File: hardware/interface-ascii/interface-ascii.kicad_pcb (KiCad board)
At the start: 2 copper layers, 88.9 x 132.1 mm, 51 parts, among them J1 Apple 2, J2 Apple 1, J3 UART, J4 Conn_01x05, J5 ISP header, J6 Keyboard, J7 SOL-20, SW1 Options, U1 ATmega328P, U2 74LS166, U3 74LS138, U4 74LS138, U5 74LS04

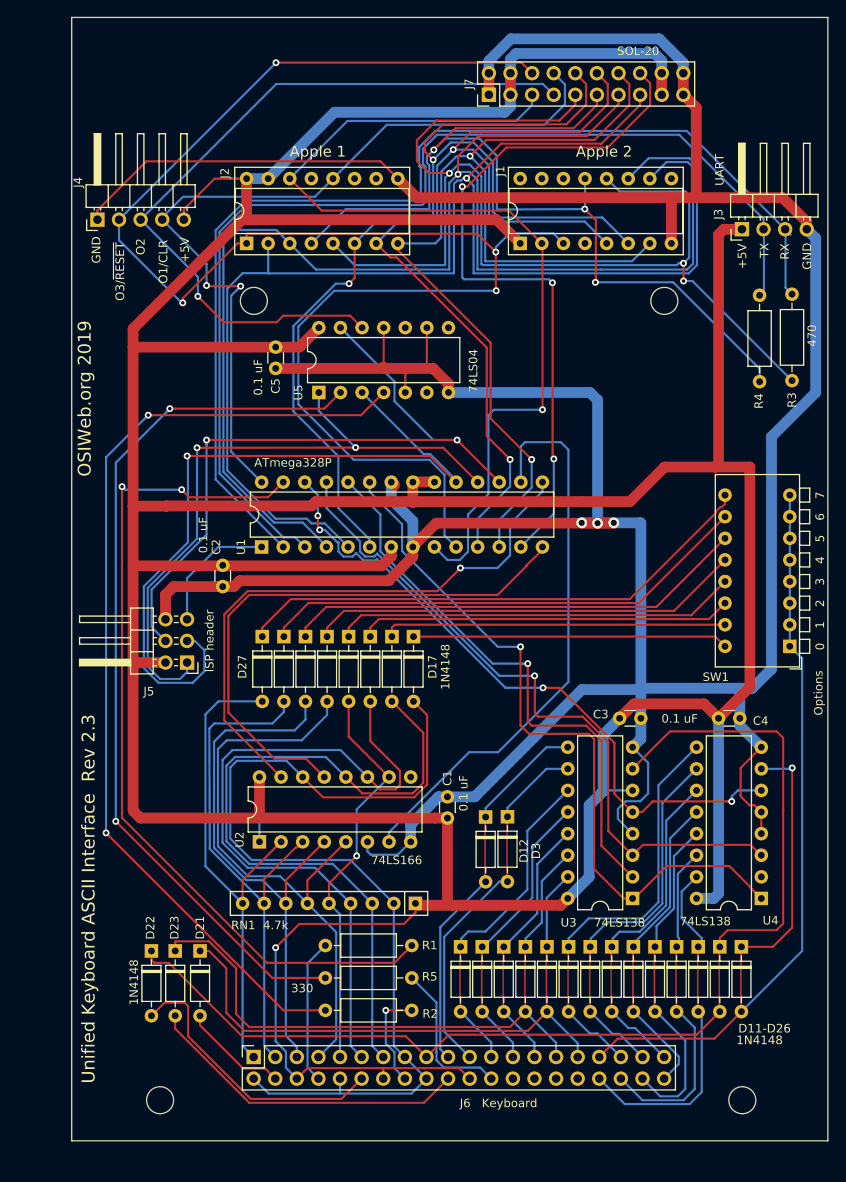
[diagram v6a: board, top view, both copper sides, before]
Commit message: PCB cleanups
- swap numbering of row select protection diodes for cleaner PCB labeling
- clarify labeling on GPIO pins on the MCU
- bump rev to 2.4 to indicate work in progress. Release will be 2.5.
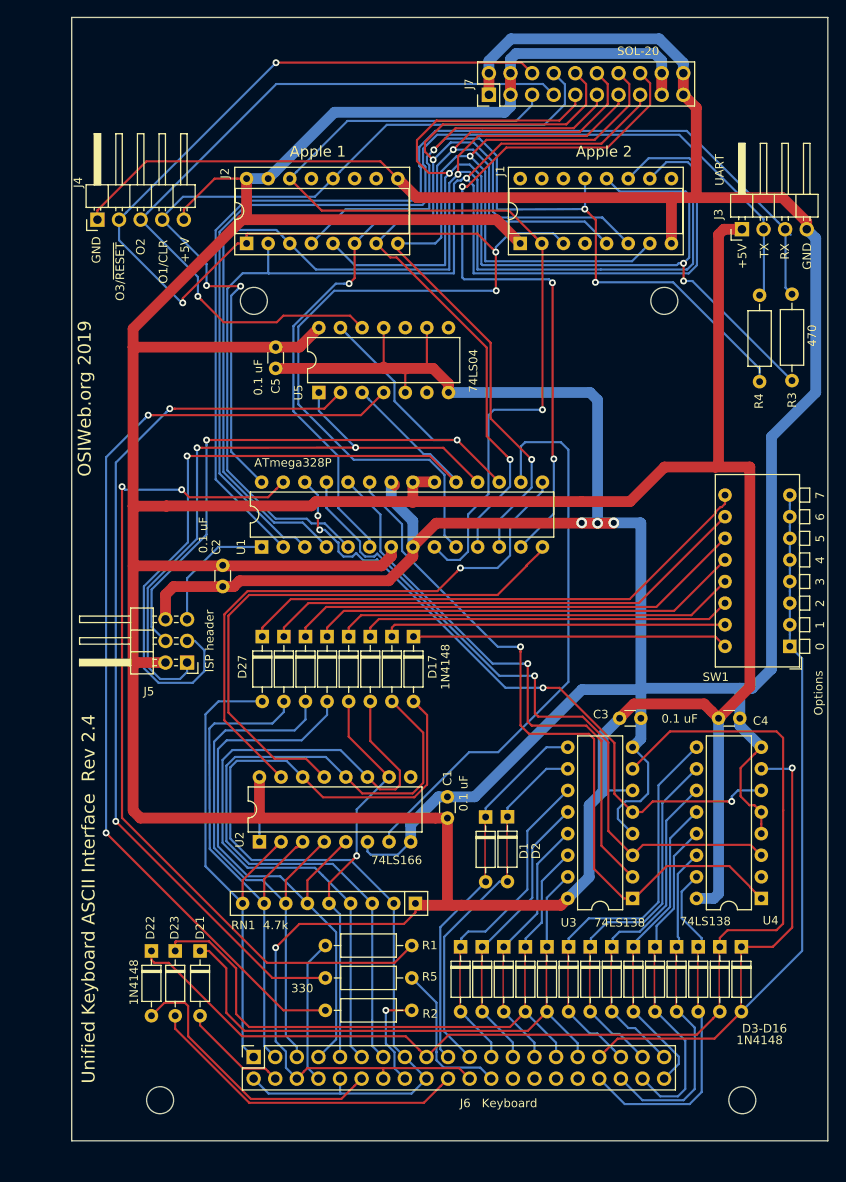
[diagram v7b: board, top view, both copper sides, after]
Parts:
- renumbered D12 to D1, D1 to D12, D3 to D2, D2 to D3
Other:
- board text added: "D3-D16"
- board text added: "Unified Keyboard ASCII Interface Rev 2.4"
- board text removed: "D11-D26"
- board text removed: "Unified Keyboard ASCII Interface Rev 2.3"
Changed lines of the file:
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@@
     (title "Unified Retro Keyboard")
     (date 2019-12-13)
-    (rev 2.3)
+    (rev 2.4)
   )
   (layers
@@
     (descr "Diode, DO-35_SOD27 series, Axial, Horizontal, pin pitch=7.62mm, , length*diameter=4*2mm^2, , http://www.diodes.com/_files/packages/DO-35.pdf")
     (tags "Diode DO-35_SOD27 series Axial Horizontal pin pitch 7.62mm  length 4mm diameter 2mm")
-    (fp_text reference D12 (at 3.9878 -4.4958 90) (layer F.SilkS)
+    (fp_text reference D1 (at 3.9878 -4.4958 90) (layer F.SilkS)
       (effects (font (size 1 1) (thickness 0.15)))
     )
@@
     )
     (pad 1 thru_hole rect (at 0 0 270) (size 1.6 1.6) (drill 0.8) (layers *.Cu *.Mask)
-      (net 48 "Net-(D12-Pad1)"))
+      (net 68 "Net-(D1-Pad1)"))
     (pad 2 thru_hole oval (at 7.62 0 270) (size 1.6 1.6) (drill 0.8) (layers *.Cu *.Mask)
       (net 24 /Row6))
@@
     (descr "Diode, DO-35_SOD27 series, Axial, Horizontal, pin pitch=7.62mm, , length*diameter=4*2mm^2, , http://www.diodes.com/_files/packages/DO-35.pdf")
     (tags "Diode DO-35_SOD27 series Axial Horizontal pin pitch 7.62mm  length 4mm diameter 2mm")
-    (fp_text reference D3 (at 4.0132 -3.3528 90) (layer F.SilkS)
+    (fp_text reference D2 (at 4.0132 -3.3528 90) (layer F.SilkS)
       (effects (font (size 1 1) (thickness 0.15)))
     )
@@
     )
     (pad 1 thru_hole rect (at 0 0 270) (size 1.6 1.6) (drill 0.8) (layers *.Cu *.Mask)
-      (net 60 "Net-(D3-Pad1)"))
+      (net 69 "Net-(D2-Pad1)"))
     (pad 2 thru_hole oval (at 7.62 0 270) (size 1.6 1.6) (drill 0.8) (layers *.Cu *.Mask)
       (net 7 /Row5))
@@
     (descr "Diode, DO-35_SOD27 series, Axial, Horizontal, pin pitch=7.62mm, , length*diameter=4*2mm^2, , http://www.diodes.com/_files/packages/DO-35.pdf")
     (tags "Diode DO-35_SOD27 series Axial Horizontal pin pitch 7.62mm  length 4mm diameter 2mm")
-    (fp_text reference D2 (at 3.81 -2.12 90) (layer F.SilkS) hide
+    (fp_text reference D3 (at 3.81 -2.12 90) (layer F.SilkS) hide
       (effects (font (size 1 1) (thickness 0.15)))
     )
@@
     )
     (pad 1 thru_hole rect (at 0 0 270) (size 1.6 1.6) (drill 0.8) (layers *.Cu *.Mask)
-      (net 69 "Net-(D2-Pad1)"))
+      (net 60 "Net-(D3-Pad1)"))
     (pad 2 thru_hole oval (at 7.62 0 270) (size 1.6 1.6) (drill 0.8) (layers *.Cu *.Mask)
       (net 3 /Row3))
@@
     (descr "Diode, DO-35_SOD27 series, Axial, Horizontal, pin pitch=7.62mm, , length*diameter=4*2mm^2, , http://www.diodes.com/_files/packages/DO-35.pdf")
     (tags "Diode DO-35_SOD27 series Axial Horizontal pin pitch 7.62mm  length 4mm diameter 2mm")
-    (fp_text reference D1 (at 3.81 -2.12 90) (layer F.SilkS) hide
+    (fp_text reference D12 (at 3.81 -2.12 90) (layer F.SilkS) hide
       (effects (font (size 1 1) (thickness 0.15)))
     )
@@
     )
     (pad 1 thru_hole rect (at 0 0 270) (size 1.6 1.6) (drill 0.8) (layers *.Cu *.Mask)
-      (net 68 "Net-(D1-Pad1)"))
+      (net 48 "Net-(D12-Pad1)"))
     (pad 2 thru_hole oval (at 7.62 0 270) (size 1.6 1.6) (drill 0.8) (layers *.Cu *.Mask)
       (net 5 /Row1))
@@
       (net 61 "Net-(D4-Pad1)"))
     (pad 14 thru_hole oval (at 7.62 5.08 180) (size 1.6 1.6) (drill 0.8) (layers *.Cu *.Mask)
-      (net 68 "Net-(D1-Pad1)"))
+      (net 48 "Net-(D12-Pad1)"))
     (pad 6 thru_hole oval (at 0 12.7 180) (size 1.6 1.6) (drill 0.8) (layers *.Cu *.Mask)
       (net 2 +5V))
@@
       (net 32 "Net-(U1-Pad26)"))
     (pad 12 thru_hole oval (at 7.62 10.16 180) (size 1.6 1.6) (drill 0.8) (layers *.Cu *.Mask)
-      (net 69 "Net-(D2-Pad1)"))
+      (net 60 "Net-(D3-Pad1)"))
     (pad 4 thru_hole oval (at 0 7.62 180) (size 1.6 1.6) (drill 0.8) (layers *.Cu *.Mask)
       (net 1 GND))
@@
       (net 27 "Net-(U1-Pad25)"))
     (pad 10 thru_hole oval (at 7.62 15.24 180) (size 1.6 1.6) (drill 0.8) (layers *.Cu *.Mask)
-      (net 60 "Net-(D3-Pad1)"))
+      (net 69 "Net-(D2-Pad1)"))
     (pad 2 thru_hole oval (at 0 2.54 180) (size 1.6 1.6) (drill 0.8) (layers *.Cu *.Mask)
       (net 28 "Net-(U1-Pad24)"))
     (pad 9 thru_hole oval (at 7.62 17.78 180) (size 1.6 1.6) (drill 0.8) (layers *.Cu *.Mask)
-      (net 48 "Net-(D12-Pad1)"))
+      (net 68 "Net-(D1-Pad1)"))
     (pad 1 thru_hole rect (at 0 0 180) (size 1.6 1.6) (drill 0.8) (layers *.Cu *.Mask)
       (net 29 "Net-(U1-Pad23)"))
@@
     (effects (font (size 1.016 1.016) (thickness 0.127)))
   )
-  (gr_text D11-D26 (at 245.2902 169.6736) (layer F.SilkS)
+  (gr_text D3-D16 (at 245.2902 169.6736) (layer F.SilkS)
     (effects (font (size 1.016 1.016) (thickness 0.127)))
   )
@@
     (effects (font (size 1.524 1.524) (thickness 0.254)))
   )
-  (gr_text "Unified Keyboard ASCII Interface  Rev 2.3" (at 165.7374 155.0178 90) (layer B.SilkS)
+  (gr_text "Unified Keyboard ASCII Interface  Rev 2.4" (at 165.7374 155.0178 90) (layer B.SilkS)
     (effects (font (size 1.524 1.524) (thickness 0.254)) (justify mirror))
   )
-  (gr_text "Unified Keyboard ASCII Interface  Rev 2.3" (at 165.8136 154.4336 90) (layer F.SilkS)
+  (gr_text "Unified Keyboard ASCII Interface  Rev 2.4" (at 165.8136 154.4336 90) (layer F.SilkS)
     (effects (font (size 1.524 1.524) (thickness 0.254)))
   )
@@
   (segment (start 210.4542 158.269) (end 209.6286 159.0946) (width 0.254) (layer B.Cu) (net 47))
   (segment (start 212.4734 158.269) (end 210.4542 158.269) (width 0.254) (layer B.Cu) (net 47))
-  (segment (start 219.649 136.6028) (end 212.4988 143.753) (width 0.254) (layer B.Cu) (net 48))
-  (segment (start 212.4988 143.753) (end 212.4988 144.807) (width 0.254) (layer B.Cu) (net 48))
-  (segment (start 222.1508 136.6028) (end 219.649 136.6028) (width 0.254) (layer B.Cu) (net 48))
+  (segment (start 219.649 136.6028) (end 212.4988 143.753) (width 0.254) (layer B.Cu) (net 68))
+  (segment (start 212.4988 143.753) (end 212.4988 144.807) (width 0.254) (layer B.Cu) (net 68))
+  (segment (start 222.1508 136.6028) (end 219.649 136.6028) (width 0.254) (layer B.Cu) (net 68))
   (segment (start 237.8988 159.0438) (end 237.8988 160.0978) (width 0.254) (layer B.Cu) (net 49))
   (segment (start 235.542861 156.687861) (end 237.8988 159.0438) (width 0.254) (layer B.Cu) (net 49))
@@
   (segment (start 232.57496 120.10804) (end 193.75116 120.10804) (width 0.254) (layer F.Cu) (net 59))
   (segment (start 240.642 112.041) (end 232.57496 120.10804) (width 0.254) (layer F.Cu) (net 59))
-  (segment (start 219.649 139.1428) (end 215.0642 143.7276) (width 0.254) (layer B.Cu) (net 60))
-  (segment (start 215.0642 143.7276) (end 215.0642 144.7816) (width 0.254) (layer B.Cu) (net 60))
-  (segment (start 222.1508 139.1428) (end 219.649 139.1428) (width 0.254) (layer B.Cu) (net 60))
+  (segment (start 219.649 139.1428) (end 215.0642 143.7276) (width 0.254) (layer B.Cu) (net 69))
+  (segment (start 215.0642 143.7276) (end 215.0642 144.7816) (width 0.254) (layer B.Cu) (net 69))
+  (segment (start 222.1508 139.1428) (end 219.649 139.1428) (width 0.254) (layer B.Cu) (net 69))
   (segment (start 247.4746 143.9942) (end 247.5 144.0196) (width 0.254) (layer F.Cu) (net 61))
   (segment (start 240.03 159.0184) (end 240.03 160.0724) (width 0.254) (layer F.Cu) (net 61))
@@
   (segment (start 218.5694 150.3442) (end 218.5694 156.1354) (width 0.254) (layer B.Cu) (net 67))
   (segment (start 222.1508 146.7628) (end 218.5694 150.3442) (width 0.254) (layer B.Cu) (net 67))
-  (segment (start 219.0648 157.2276) (end 217.1978 159.0946) (width 0.254) (layer B.Cu) (net 68))
-  (segment (start 219.1028 157.2276) (end 219.0648 157.2276) (width 0.254) (layer B.Cu) (net 68))
-  (segment (start 217.1978 159.0946) (end 217.1978 160.1486) (width 0.254) (layer B.Cu) (net 68))
-  (segment (start 219.1028 152.3508) (end 219.1028 157.2276) (width 0.254) (layer B.Cu) (net 68))
-  (segment (start 222.1508 149.3028) (end 219.1028 152.3508) (width 0.254) (layer B.Cu) (net 68))
-  (segment (start 217.9852 154.3066) (end 212.1432 160.1486) (width 0.254) (layer B.Cu) (net 69))
-  (segment (start 217.9852 148.3884) (end 217.9852 154.3066) (width 0.254) (layer B.Cu) (net 69))
-  (segment (start 222.1508 144.2228) (end 217.9852 148.3884) (width 0.254) (layer B.Cu) (net 69))
+  (segment (start 219.0648 157.2276) (end 217.1978 159.0946) (width 0.254) (layer B.Cu) (net 48))
+  (segment (start 219.1028 157.2276) (end 219.0648 157.2276) (width 0.254) (layer B.Cu) (net 48))
+  (segment (start 217.1978 159.0946) (end 217.1978 160.1486) (width 0.254) (layer B.Cu) (net 48))
+  (segment (start 219.1028 152.3508) (end 219.1028 157.2276) (width 0.254) (layer B.Cu) (net 48))
+  (segment (start 222.1508 149.3028) (end 219.1028 152.3508) (width 0.254) (layer B.Cu) (net 48))
+  (segment (start 217.9852 154.3066) (end 212.1432 160.1486) (width 0.254) (layer B.Cu) (net 60))
+  (segment (start 217.9852 148.3884) (end 217.9852 154.3066) (width 0.254) (layer B.Cu) (net 60))
+  (segment (start 222.1508 144.2228) (end 217.9852 148.3884) (width 0.254) (layer B.Cu) (net 60))
   (segment (start 186.578999 174.386199) (end 186.909201 174.716401) (width 0.254) (layer F.Cu) (net 70))
   (segment (start 183.999829 174.386199) (end 186.578999 174.386199) (width 0.254) (layer F.Cu) (net 70))

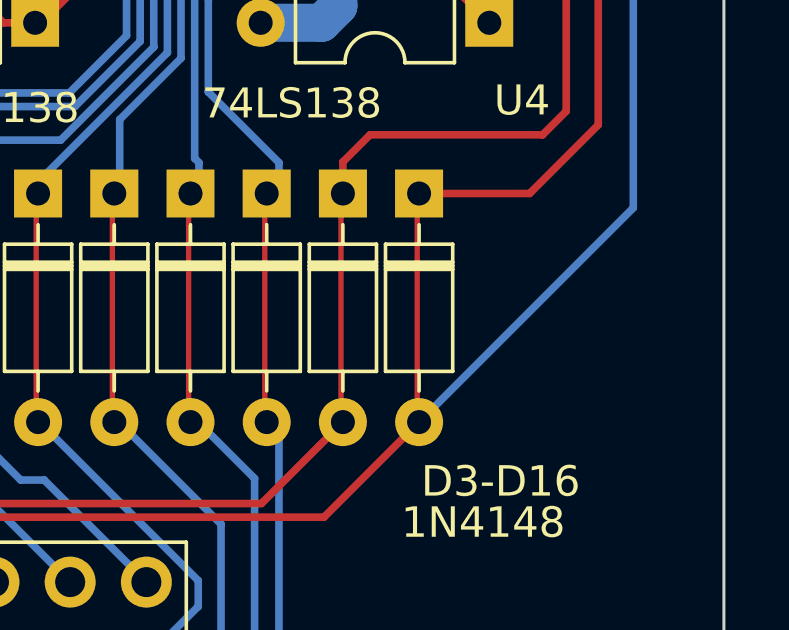
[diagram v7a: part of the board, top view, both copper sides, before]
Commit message: Move DIP switch to row 8 (9th row)
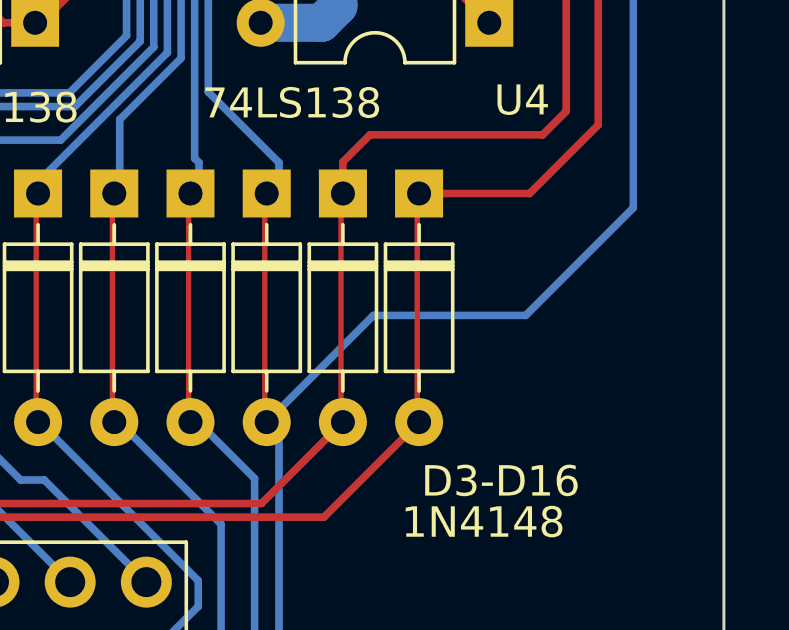
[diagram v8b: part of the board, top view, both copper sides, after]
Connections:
- SW1 pad 1: /Row15 -> /Row8
- SW1 pad 2: /Row15 -> /Row8
- SW1 pad 3: /Row15 -> /Row8
- SW1 pad 4: /Row15 -> /Row8
- SW1 pad 5: /Row15 -> /Row8
- SW1 pad 6: /Row15 -> /Row8
- SW1 pad 7: /Row15 -> /Row8
- SW1 pad 8: /Row15 -> /Row8
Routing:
- net /Row8: track 23.3 -> 92.7 mm
- net /Row15: track 83.2 -> 18.9 mm
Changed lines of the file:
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@@
     (thickness 1.6)
     (drawings 33)
-    (tracks 1119)
+    (tracks 1121)
     (zones 0)
     (modules 51)
@@
     )
     (pad 1 thru_hole rect (at 0 0 180) (size 1.6 1.6) (drill 0.8) (layers *.Cu *.Mask)
-      (net 38 /Row15))
+      (net 37 /Row8))
     (pad 9 thru_hole oval (at 7.62 17.78 180) (size 1.6 1.6) (drill 0.8) (layers *.Cu *.Mask)
       (net 73 "Net-(D27-Pad1)"))
     (pad 2 thru_hole oval (at 0 2.54 180) (size 1.6 1.6) (drill 0.8) (layers *.Cu *.Mask)
-      (net 38 /Row15))
+      (net 37 /Row8))
     (pad 10 thru_hole oval (at 7.62 15.24 180) (size 1.6 1.6) (drill 0.8) (layers *.Cu *.Mask)
       (net 56 "Net-(D20-Pad1)"))
     (pad 3 thru_hole oval (at 0 5.08 180) (size 1.6 1.6) (drill 0.8) (layers *.Cu *.Mask)
-      (net 38 /Row15))
+      (net 37 /Row8))
     (pad 11 thru_hole oval (at 7.62 12.7 180) (size 1.6 1.6) (drill 0.8) (layers *.Cu *.Mask)
       (net 59 "Net-(D26-Pad1)"))
     (pad 4 thru_hole oval (at 0 7.62 180) (size 1.6 1.6) (drill 0.8) (layers *.Cu *.Mask)
-      (net 38 /Row15))
+      (net 37 /Row8))
     (pad 12 thru_hole oval (at 7.62 10.16 180) (size 1.6 1.6) (drill 0.8) (layers *.Cu *.Mask)
       (net 55 "Net-(D19-Pad1)"))
     (pad 5 thru_hole oval (at 0 10.16 180) (size 1.6 1.6) (drill 0.8) (layers *.Cu *.Mask)
-      (net 38 /Row15))
+      (net 37 /Row8))
     (pad 13 thru_hole oval (at 7.62 7.62 180) (size 1.6 1.6) (drill 0.8) (layers *.Cu *.Mask)
       (net 58 "Net-(D25-Pad1)"))
     (pad 6 thru_hole oval (at 0 12.7 180) (size 1.6 1.6) (drill 0.8) (layers *.Cu *.Mask)
-      (net 38 /Row15))
+      (net 37 /Row8))
     (pad 14 thru_hole oval (at 7.62 5.08 180) (size 1.6 1.6) (drill 0.8) (layers *.Cu *.Mask)
       (net 54 "Net-(D18-Pad1)"))
     (pad 7 thru_hole oval (at 0 15.24 180) (size 1.6 1.6) (drill 0.8) (layers *.Cu *.Mask)
-      (net 38 /Row15))
+      (net 37 /Row8))
     (pad 15 thru_hole oval (at 7.62 2.54 180) (size 1.6 1.6) (drill 0.8) (layers *.Cu *.Mask)
       (net 57 "Net-(D24-Pad1)"))
     (pad 8 thru_hole oval (at 0 17.78 180) (size 1.6 1.6) (drill 0.8) (layers *.Cu *.Mask)
-      (net 38 /Row15))
+      (net 37 /Row8))
     (pad 16 thru_hole oval (at 7.62 0 180) (size 1.6 1.6) (drill 0.8) (layers *.Cu *.Mask)
       (net 53 "Net-(D17-Pad1)"))
@@
   (segment (start 239.401378 170.861022) (end 228.024578 170.861022) (width 0.254) (layer F.Cu) (net 38))
   (segment (start 228.024578 170.861022) (end 226.709199 172.176401) (width 0.254) (layer F.Cu) (net 38))
-  (segment (start 248.262 106.961) (end 248.262 108.09237) (width 0.254) (layer B.Cu) (net 38))
-  (segment (start 248.262 108.09237) (end 248.262 109.501) (width 0.254) (layer B.Cu) (net 38))
-  (segment (start 248.262 122.201) (end 248.262 123.33237) (width 0.254) (layer B.Cu) (net 38))
-  (segment (start 248.262 123.33237) (end 248.262 124.741) (width 0.254) (layer B.Cu) (net 38))
-  (segment (start 248.262 119.661) (end 248.262 122.201) (width 0.254) (layer B.Cu) (net 38))
-  (segment (start 248.262 117.121) (end 248.262 118.25237) (width 0.254) (layer B.Cu) (net 38))
-  (segment (start 248.262 118.25237) (end 248.262 119.661) (width 0.254) (layer B.Cu) (net 38))
-  (segment (start 248.262 114.581) (end 248.262 115.71237) (width 0.254) (layer B.Cu) (net 38))
-  (segment (start 248.262 115.71237) (end 248.262 117.121) (width 0.254) (layer B.Cu) (net 38))
-  (segment (start 248.262 112.041) (end 248.262 114.581) (width 0.254) (layer B.Cu) (net 38))
-  (segment (start 248.262 109.501) (end 248.262 110.63237) (width 0.254) (layer B.Cu) (net 38))
-  (segment (start 248.262 110.63237) (end 248.262 112.041) (width 0.254) (layer B.Cu) (net 38))
-  (segment (start 249.7098 160.5526) (end 242.57 167.6924) (width 0.254) (layer B.Cu) (net 38))
-  (segment (start 249.7098 126.1888) (end 249.7098 160.5526) (width 0.254) (layer B.Cu) (net 38))
-  (segment (start 248.262 124.741) (end 249.7098 126.1888) (width 0.254) (layer B.Cu) (net 38))
+  (segment (start 248.262 106.961) (end 248.262 108.09237) (width 0.254) (layer B.Cu) (net 37))
+  (segment (start 248.262 108.09237) (end 248.262 109.501) (width 0.254) (layer B.Cu) (net 37))
+  (segment (start 248.262 122.201) (end 248.262 123.33237) (width 0.254) (layer B.Cu) (net 37))
+  (segment (start 248.262 123.33237) (end 248.262 124.741) (width 0.254) (layer B.Cu) (net 37))
+  (segment (start 248.262 119.661) (end 248.262 122.201) (width 0.254) (layer B.Cu) (net 37))
+  (segment (start 248.262 117.121) (end 248.262 118.25237) (width 0.254) (layer B.Cu) (net 37))
+  (segment (start 248.262 118.25237) (end 248.262 119.661) (width 0.254) (layer B.Cu) (net 37))
+  (segment (start 248.262 114.581) (end 248.262 115.71237) (width 0.254) (layer B.Cu) (net 37))
+  (segment (start 248.262 115.71237) (end 248.262 117.121) (width 0.254) (layer B.Cu) (net 37))
+  (segment (start 248.262 112.041) (end 248.262 114.581) (width 0.254) (layer B.Cu) (net 37))
+  (segment (start 248.262 109.501) (end 248.262 110.63237) (width 0.254) (layer B.Cu) (net 37))
+  (segment (start 248.262 110.63237) (end 248.262 112.041) (width 0.254) (layer B.Cu) (net 37))
+  (segment (start 249.7098 126.1888) (end 249.7098 160.5526) (width 0.254) (layer B.Cu) (net 37))
+  (segment (start 248.262 124.741) (end 249.7098 126.1888) (width 0.254) (layer B.Cu) (net 37))
+  (segment (start 249.7098 160.5526) (end 246.126 164.1364) (width 0.254) (layer B.Cu) (net 37))
+  (segment (start 241.046 164.1364) (end 237.49 167.6924) (width 0.254) (layer B.Cu) (net 37))
+  (segment (start 246.126 164.1364) (end 241.046 164.1364) (width 0.254) (layer B.Cu) (net 37))
   (segment (start 224.7416 170.2578) (end 225.6306 170.2578) (width 0.254) (layer B.Cu) (net 39))
   (segment (start 227.549201 172.176401) (end 228.3992 173.0264) (width 0.254) (layer B.Cu) (net 39))
